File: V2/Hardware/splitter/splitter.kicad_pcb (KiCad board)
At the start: 2 copper layers, 21 parts, among them J0 Rpi_40Pin_F, J1 Control_seg:1, J2 Control_seg:2, J3 Control_seg:3, J4 Molex_PSU_F, J5 Siren, J6 USB_A_F, K0 RELRAS0515, Q1 BD139-16

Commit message: Update files
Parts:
- C1: value 4700uF 25V LOW ESR -> 220uF 25V LOW ESR; footprint Capacitor_THT:CP_Radial_D18.0mm_P7.50mm -> Capacitor_THT:CP_Radial_D8.0mm_P3.50mm
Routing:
- net Earth: track 202.2 -> 174.8 mm
- net Net-(J0-Pad17): track 0.00 -> 3.80 mm
- net Net-(J0-Pad2): track 0.00 -> 3.74 mm
- net Net-(J0-Pad9): track 0.00 -> 3.72 mm
- net Net-(J0-Pad25): track 0.00 -> 3.48 mm
- net Net-(J0-Pad5): track 0.00 -> 3.40 mm
- net Net-(J0-Pad3): track 0.00 -> 3.36 mm
- net Net-(J0-Pad14): track 0.00 -> 2.96 mm
- net Net-(J0-Pad1): track 0.00 -> 2.92 mm
- net Net-(J0-Pad18): track 0.00 -> 2.88 mm
- net Net-(J0-Pad10): track 0.00 -> 2.80 mm
- net Net-(J0-Pad22): track 0.00 -> 2.72 mm
- net Net-(J0-Pad34): track 0.00 -> 2.62 mm
- net Net-(J0-Pad38): track 0.00 -> 2.54 mm
- net Net-(J0-Pad6): track 0.00 -> 2.48 mm
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
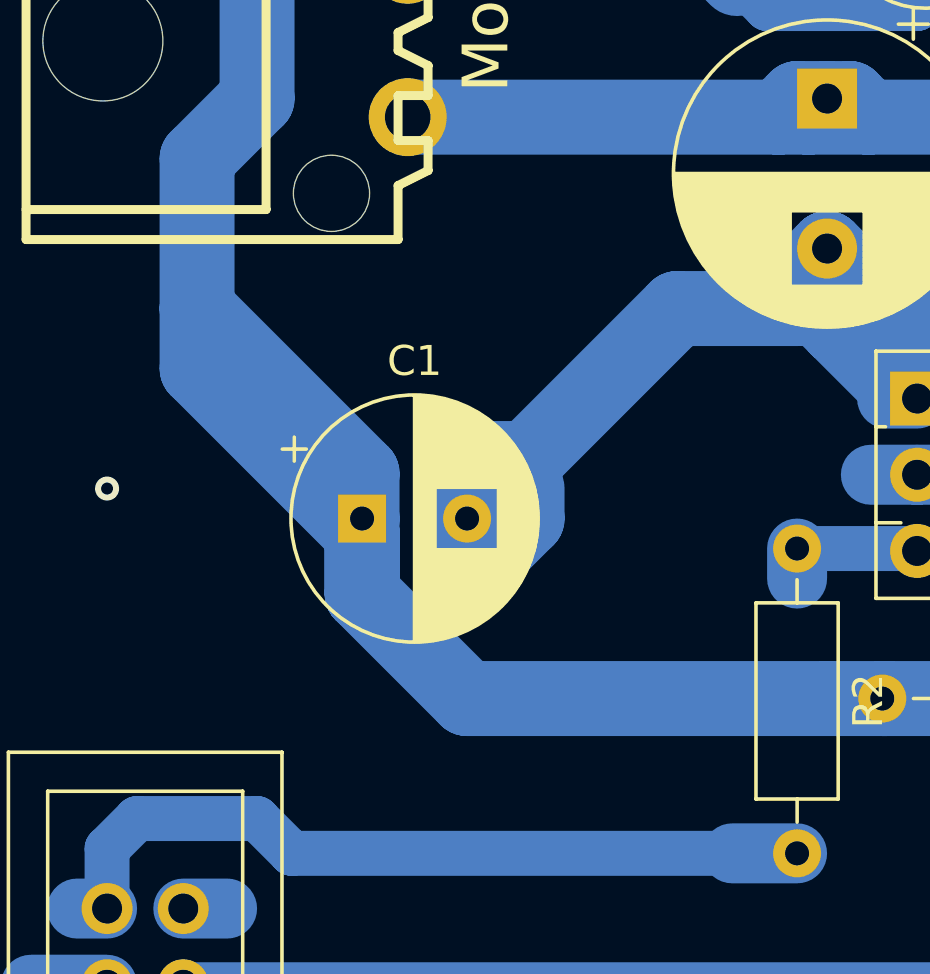
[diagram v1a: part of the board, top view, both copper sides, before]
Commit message: update capacitors
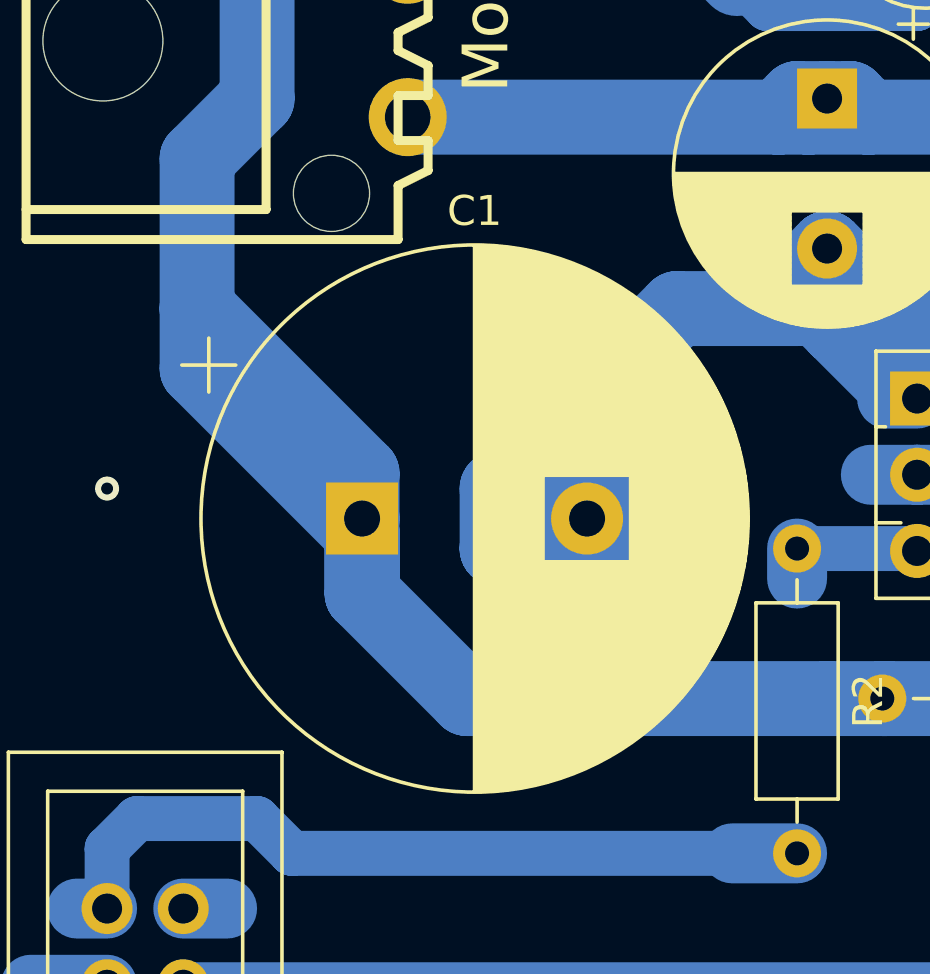
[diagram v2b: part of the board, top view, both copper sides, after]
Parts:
- C1: value 220uF 25V LOW ESR -> 4700uF 25V LOW ESR; footprint Capacitor_THT:CP_Radial_D8.0mm_P3.50mm -> Capacitor_THT:CP_Radial_D18.0mm_P7.50mm
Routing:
- net Earth: track 174.8 -> 190.1 mm

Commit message: Update splitter
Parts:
- removed C1: 4700uF 25V LOW ESR, Capacitor_THT:CP_Radial_D18.0mm_P7.50mm
- removed C2: 220nF, Capacitor_THT:C_Disc_D4.3mm_W1.9mm_P5.00mm
- removed D3: LED_2V_20mA, LED_THT:LED_D5.0mm
- removed the J5 at (174.0, 83.0)
- removed R3, R4: 33k, Resistor_THT:R_Axial_DIN0207_L6.3mm_D2.5mm_P10.16mm_Horizontal
- added J6: Siren, TerminalBlock_RND:TerminalBlock_RND_205-00067_1x02_P7.50mm_Horizontal, F.Cu at (176.0, 79.0)
- added J7: Siren, TerminalBlock_RND:TerminalBlock_RND_205-00067_1x02_P7.50mm_Horizontal, F.Cu at (176.0, 46.0)
- added R1: 33k, Resistor_THT:R_Axial_DIN0207_L6.3mm_D2.5mm_P10.16mm_Horizontal, F.Cu at (137.0, 68.0)
- moved D2 28.2 mm to (137.0, 75.0), turned to 90 degrees
- moved C0 11.7 mm to (149.0, 47.0)
- moved D0 11.2 mm to (139.0, 50.5)
- moved R0 11.1 mm to (145.0, 43.0)
- moved J1 7.00 mm to (172.0, 126.0)
- moved J2 7.00 mm to (172.0, 111.0)
- moved J3 7.00 mm to (172.0, 95.0)
- moved J5 1.41 mm to (163.0, 50.0), turned to 180 degrees
- moved K0 1.00 mm to (161.0, 66.0)
- renumbered J6 to J5
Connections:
- D2 pad 1: Net-(D2-Pad1) -> Net-(D1-Pad2)
- K0 pad 11: Earth -> Net-(J7-Pad1)
- K0 pad 14: Net-(D2-Pad1) -> /230V-L
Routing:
- net /5V+: track 57.8 -> 178.5 mm
- net /12V+: track 116.5 -> 8.35 mm
- net Net-(D2-Pad1): track 47.1 -> 0.00 mm
- net Net-(J7-Pad1): track 0.00 -> 44.6 mm
- net /230V-N: track 0.00 -> 42.1 mm
- net Earth: track 190.1 -> 220.0 mm
- net Net-(D1-Pad2): track 40.0 -> 64.1 mm
- net /230V-L: track 0.00 -> 24.1 mm
- net Net-(Q1-Pad3): track 5.95 -> 22.8 mm
- net Net-(D3-Pad2): track 12.0 -> 0.00 mm
- net /seg:2_bit:a_gpio:10: track 51.0 -> 58.3 mm
- net /seg:3_bit:c_gpio:19: track 44.0 -> 51.0 mm
- net /seg:3_bit:b_gpio:13: track 44.0 -> 51.0 mm
- net /seg:2_bit:d_gpio:05: track 46.4 -> 53.4 mm
- net /seg:2_bit:c_gpio:11: track 44.3 -> 51.3 mm
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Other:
- board text added: "67mm"
- board text removed: "61mm"

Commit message: revision 2 boards
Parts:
- added H1: MountingHole, myFP:MountingHole_2.75mm_NoPad, F.Cu at (54.7, 127.8)
- added H2: MountingHole, myFP:MountingHole_2.75mm_NoPad, F.Cu at (54.7, 69.8)
- added H3: MountingHole, myFP:MountingHole_2.75mm_NoPad, F.Cu at (77.7, 127.8)
- added H4: MountingHole, myFP:MountingHole_2.75mm_NoPad, F.Cu at (77.7, 69.8)
- added H5: MountingHole, myFP:MountingHole_2.75mm_NoPad, F.Cu at (103.7, 127.8)
- added H6: MountingHole, myFP:MountingHole_2.75mm_NoPad, F.Cu at (103.7, 69.8)
- added Screw: MountingHole_3.2mm_M3, MountingHole:MountingHole_3.2mm_M3, F.Cu at (77.0, 145.0)
- added Screw: MountingHole_3.2mm_M3, MountingHole:MountingHole_3.2mm_M3, F.Cu at (70.0, 185.0)
- added Screw: MountingHole_3.2mm_M3, MountingHole:MountingHole_3.2mm_M3, F.Cu at (122.0, 155.0)
- added Screw: MountingHole_3.2mm_M3, MountingHole:MountingHole_3.2mm_M3, F.Cu at (110.0, 32.0)
- added Screw: MountingHole_3.2mm_M3, MountingHole:MountingHole_3.2mm_M3, F.Cu at (55.0, 32.0)
- J0: footprint Connector_IDC:IDC-Header_2x20_P2.54mm_Vertical -> Connector_PinSocket_2.54mm:PinSocket_2x20_P2.54mm_Vertical
- J1, J2, J3: footprint Connector_PinHeader_2.54mm:PinHeader_2x03_P2.54mm_Horizontal -> Connector_IDC:IDC-Header_2x05-1MP_P2.54mm_Latch_Vertical
- J4: footprint PSU:conn_hdd_15-24-4441 -> KicadLib:conn_hdd_15-24-4449
- moved J7 181.6 mm to (58.0, 184.0), turned to 90 degrees
- moved J5 152.6 mm to (83.0, 180.0), turned to 0 degrees
- moved R0 150.6 mm to (101.0, 187.0), turned to 90 degrees
- moved C0 145.6 mm to (97.0, 183.0), turned to 270 degrees
- moved J6 138.2 mm to (58.0, 151.0), turned to 90 degrees
- moved D1 133.6 mm to (78.0, 169.0), turned to 90 degrees
- moved D0 132.8 mm to (107.0, 179.5), turned to 270 degrees
- moved K0 131.7 mm to (73.0, 164.0), turned to 180 degrees
- moved J4 130.1 mm to (121.0, 180.0), turned to 90 degrees
- moved C3 124.8 mm to (100.0, 173.0), turned to 90 degrees
- moved Q1 109.2 mm to (97.0, 163.0), turned to 90 degrees
- moved J1 100.4 mm to (122.0, 38.9)
- moved R1 98.1 mm to (109.0, 162.0), turned to 270 degrees
- moved R2 96.6 mm to (101.0, 158.0), turned to 90 degrees
- moved J0 89.5 mm to (56.0, 74.7), turned to 0 degrees
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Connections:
- J1 pad 1: /seg:1_bit:d_gpio:22 -> /seg:1_bit:a_gpio:04
- J1 pad 2: Net-(J1-Pad2) -> Earth
- J1 pad 3: /seg:1_bit:c_gpio:27 -> /seg:1_bit:b_gpio:17
- J1 pad 4: Net-(J1-Pad4) -> Earth
- J1 pad 5: /seg:1_bit:b_gpio:17 -> /seg:1_bit:c_gpio:27
- J1 pad 6: /seg:1_bit:a_gpio:04 -> Earth
- J2 pad 1: /seg:2_bit:d_gpio:05 -> /seg:2_bit:a_gpio:10
- J2 pad 2: Net-(J2-Pad2) -> Earth
- J2 pad 3: /seg:2_bit:c_gpio:11 -> /seg:2_bit:b_gpio:09
- J2 pad 4: Net-(J2-Pad4) -> Earth
- J2 pad 5: /seg:2_bit:b_gpio:09 -> /seg:2_bit:c_gpio:11
- J2 pad 6: /seg:2_bit:a_gpio:10 -> Earth
- J3 pad 1: /seg:3_bit:d_gpio:26 -> /seg:3_bit:a_gpio:06
- J3 pad 2: Net-(J3-Pad2) -> Earth
- J3 pad 3: /seg:3_bit:c_gpio:19 -> /seg:3_bit:b_gpio:13
- J3 pad 4: Net-(J3-Pad4) -> Earth
- J3 pad 5: /seg:3_bit:b_gpio:13 -> /seg:3_bit:c_gpio:19
- J3 pad 6: /seg:3_bit:a_gpio:06 -> Earth
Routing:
- net Earth: track 220.0 -> 443.5 mm
- net /5V+: track 178.5 -> 255.8 mm
- net /SIREN_gpio:21: track 28.7 -> 70.7 mm
- net /seg:1_bit:a_gpio:04: track 57.2 -> 93.3 mm
- net /seg:1_bit:d_gpio:22: track 52.2 -> 85.0 mm
- net /seg:1_bit:c_gpio:27: track 52.2 -> 85.0 mm
- net /seg:1_bit:b_gpio:17: track 52.2 -> 85.0 mm
- net /seg:2_bit:d_gpio:05: track 53.4 -> 75.0 mm
- net /seg:2_bit:b_gpio:09: track 51.3 -> 72.9 mm
- net /seg:2_bit:c_gpio:11: track 51.3 -> 72.9 mm
- net /seg:3_bit:d_gpio:26: track 51.0 -> 72.2 mm
- net /seg:3_bit:b_gpio:13: track 51.0 -> 71.7 mm
- net /seg:3_bit:c_gpio:19: track 51.0 -> 70.2 mm
- net /seg:3_bit:a_gpio:06: track 57.0 -> 72.3 mm
- net /seg:2_bit:a_gpio:10: track 58.3 -> 72.9 mm
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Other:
- board text added: "167 mm"
- board text added: "81 mm"
- board text removed: "100mm"
- board text removed: "67mm"
- board text removed: "SEG1"
- board text removed: "SEG2"
- board text removed: "SEG3"

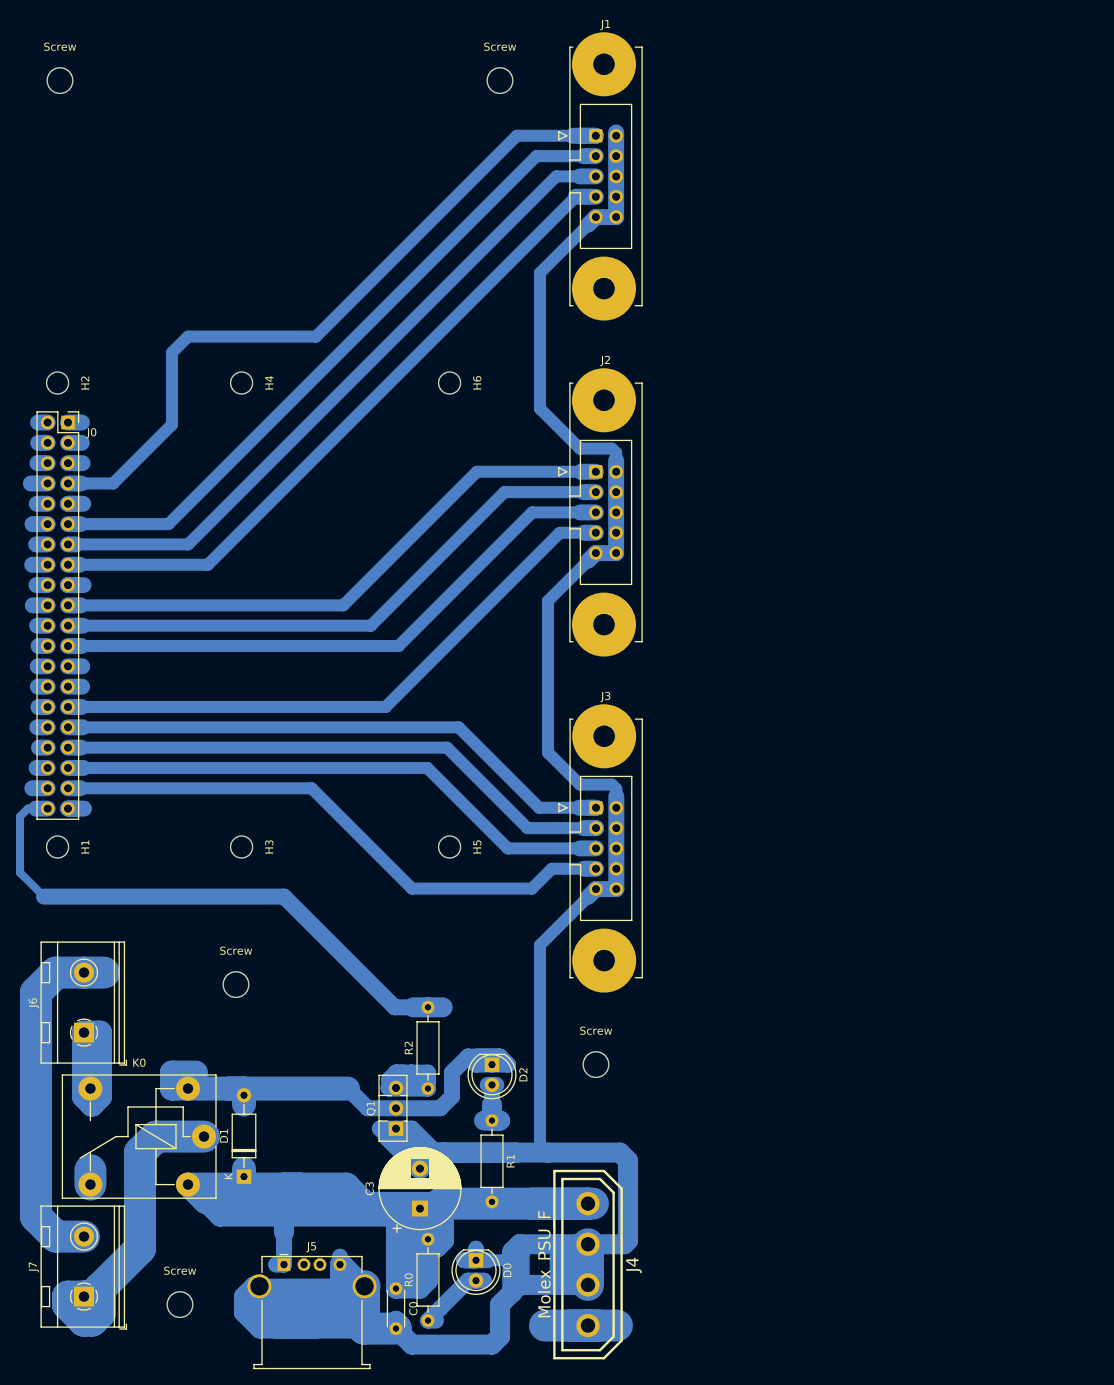
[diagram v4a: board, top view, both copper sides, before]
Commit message: Remove version 1 board
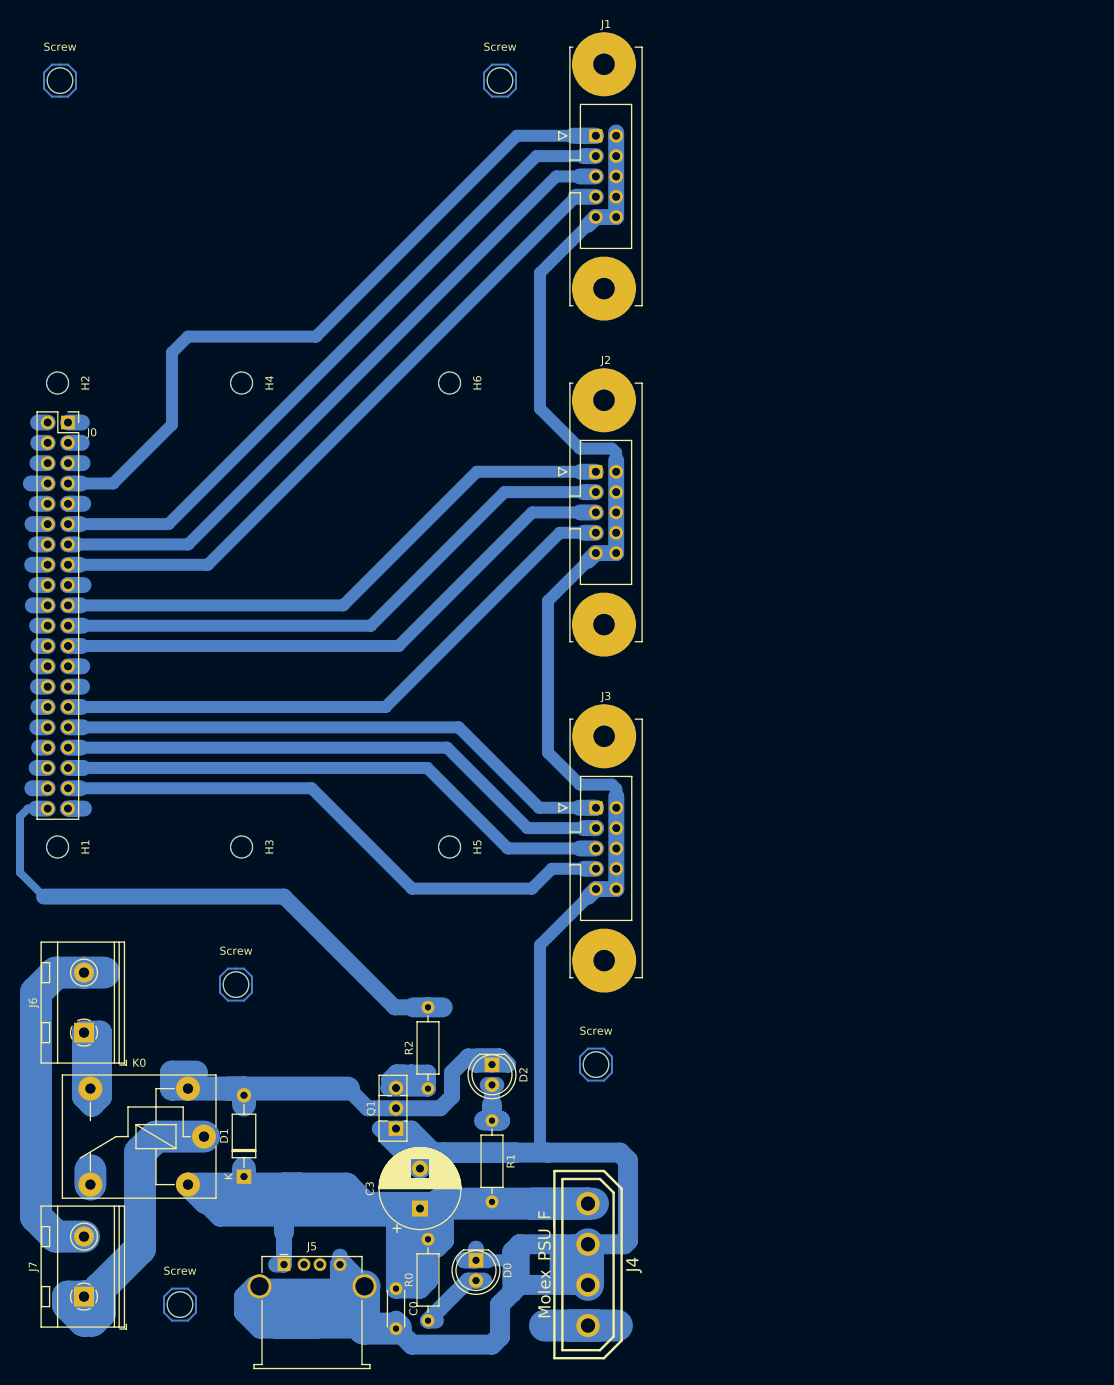
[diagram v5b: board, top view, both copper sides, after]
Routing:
- net (no net): track 0.00 -> 68.3 mm, vias 0 -> 11
